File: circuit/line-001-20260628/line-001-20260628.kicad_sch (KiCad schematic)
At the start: 200 parts, among them J1 Conn_01x02_Pin, J2 Conn_01x02_Pin, J3 Conn_02x03_Odd_Even, P1 USB-typeC, SW1 SW_DPDT, SW2 SW_Push, U1 LM339DR, U10 LM339DR, U11 LM339DR, U12 LM339DR, U13 LM339DR, U14 LM339DR, U15 LM339DR, U16 LM339DR, U17 ATmega2560-16A, U18 CH340G, U2 LM339DR, U3 LM339DR, U4 LM339DR, U5 LM339DR, U6 LM339DR, U7 LM339DR, U8 LM339DR, U9 LM339DR, Y1 16MHz, Y2 12MHz

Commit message: Update ラインセンサ基板の回路図のDR完了
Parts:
- removed C12, C8: 0.1u, symbol Device:C
- removed C13: 10u, symbol Device:C
- removed C17, C18: 100n, symbol Device:C
- removed D10, D16, D17, D18, D19, D2, D20, D26, D27, D28, D29, D30, D36, D37, D38, D39, D4, D40, D46, D47, D48, D49, D50, D56, D57, D58, D59, D6, D60, D66, D67, D69, D70, D71, D72, D8: D_Photo, symbol Device:D_Photo
- removed SW1: SW_DPDT, symbol Switch:SW_DPDT_x2
- added C1, C10, C11, C12, C13, C14, C15, C16, C2, C24, C3, C31, C33, C4, C5, C6, C7, C8, C9: 100n, Capacitor_SMD:C_0805_2012Metric, symbol Device:C_Small
- added D37: D40, LED_SMD:LED_0603_1608Metric, symbol Device:LED_Small
- added D38: D41, LED_SMD:LED_0603_1608Metric, symbol Device:LED_Small
- added Q1, Q10, Q11, Q12, Q13, Q14, Q15, Q16, Q17, Q18, Q19, Q2, Q20, Q21, Q22, Q23, Q24, Q25, Q26, Q27, Q28, Q29, Q3, Q30, Q31, Q32, Q33, Q34, Q35, Q36, Q4, Q5, Q6, Q7, Q8, Q9: NJL7502L, @Thrive_footprint_kicker:NJL7502L, symbol Device:Q_Photo_NPN_CE
- added R79, R80: 330, Resistor_SMD:R_0805_2012Metric, symbol Device:R_Small
- C17: renamed from C10; value C -> 22p; footprint (none) -> Capacitor_SMD:C_0805_2012Metric
- C18: renamed from C9; footprint (none) -> Capacitor_SMD:C_0805_2012Metric
- C19: renamed from C11; value C -> 22p; footprint (none) -> Capacitor_SMD:C_0805_2012Metric
- C20: renamed from C14; value 100u -> 470; footprint (none) -> Capacitor_SMD:C_0805_2012Metric
- C21: renamed from C1; value 10u -> 10μ; footprint (none) -> Capacitor_SMD:C_0805_2012Metric
- C22: renamed from C2; value 10u -> 10μ; footprint (none) -> Capacitor_SMD:C_0805_2012Metric
- C23: renamed from C5; value 0.1u -> 100n; footprint (none) -> Capacitor_SMD:C_0805_2012Metric
- C25: renamed from C6; value 0.1u -> 100n; footprint (none) -> Capacitor_SMD:C_0805_2012Metric
- C26: renamed from C7; value 0.1u -> 100n; footprint (none) -> Capacitor_SMD:C_0805_2012Metric
- C27: renamed from C3; value 10u -> 10μ; footprint (none) -> Capacitor_SMD:C_0805_2012Metric
- C28: renamed from C4; value 10u -> 10μ; footprint (none) -> Capacitor_SMD:C_0805_2012Metric
- C29: renamed from C15; footprint (none) -> Capacitor_SMD:C_0805_2012Metric
- C30: renamed from C16; footprint (none) -> Capacitor_SMD:C_0805_2012Metric
- C32: renamed from C19; footprint (none) -> Capacitor_SMD:C_0805_2012Metric
- D1: footprint (none) -> LED_THT:LED_D3.0mm
- D10: renamed from D15; footprint (none) -> LED_THT:LED_D3.0mm
- D11: renamed from D21; footprint (none) -> LED_THT:LED_D3.0mm
- D12: renamed from D22; footprint (none) -> LED_THT:LED_D3.0mm
- D13: renamed from D23; footprint (none) -> LED_THT:LED_D3.0mm
- D14: renamed from D24; footprint (none) -> LED_THT:LED_D3.0mm
- D15: renamed from D25; footprint (none) -> LED_THT:LED_D3.0mm
- D16: renamed from D31; footprint (none) -> LED_THT:LED_D3.0mm
- D17: renamed from D32; footprint (none) -> LED_THT:LED_D3.0mm
- D18: renamed from D33; footprint (none) -> LED_THT:LED_D3.0mm
- D19: renamed from D34; footprint (none) -> LED_THT:LED_D3.0mm
- D2: renamed from D3; footprint (none) -> LED_THT:LED_D3.0mm
- D20: renamed from D35; footprint (none) -> LED_THT:LED_D3.0mm
- D21: renamed from D41; footprint (none) -> LED_THT:LED_D3.0mm
- D22: renamed from D42; footprint (none) -> LED_THT:LED_D3.0mm
- D23: renamed from D43; footprint (none) -> LED_THT:LED_D3.0mm
- D24: renamed from D44; footprint (none) -> LED_THT:LED_D3.0mm
- D25: renamed from D45; footprint (none) -> LED_THT:LED_D3.0mm
- D26: renamed from D51; footprint (none) -> LED_THT:LED_D3.0mm
- D27: renamed from D52; footprint (none) -> LED_THT:LED_D3.0mm
- D28: renamed from D53; footprint (none) -> LED_THT:LED_D3.0mm
- D29: renamed from D54; footprint (none) -> LED_THT:LED_D3.0mm
- D3: renamed from D5; footprint (none) -> LED_THT:LED_D3.0mm
- D30: renamed from D55; footprint (none) -> LED_THT:LED_D3.0mm
- D31: renamed from D61; footprint (none) -> LED_THT:LED_D3.0mm
- D32: renamed from D62; footprint (none) -> LED_THT:LED_D3.0mm
- D33: renamed from D63; footprint (none) -> LED_THT:LED_D3.0mm
- D34: renamed from D64; footprint (none) -> LED_THT:LED_D3.0mm
- D35: renamed from D65; footprint (none) -> LED_THT:LED_D3.0mm
- D36: renamed from D68; footprint (none) -> LED_THT:LED_D3.0mm
- D4: renamed from D7; footprint (none) -> LED_THT:LED_D3.0mm
- D5: renamed from D9; footprint (none) -> LED_THT:LED_D3.0mm
- D6: renamed from D11; footprint (none) -> LED_THT:LED_D3.0mm
- D7: renamed from D12; footprint (none) -> LED_THT:LED_D3.0mm
- D8: renamed from D13; footprint (none) -> LED_THT:LED_D3.0mm
- D9: renamed from D14; footprint (none) -> LED_THT:LED_D3.0mm
- J1: value Conn_01x02_Pin -> Relay_{Power}
- J2: value Conn_01x02_Pin -> Relay_{Signal}
- J3: value Conn_02x03_Odd_Even -> ICSP_{Arduino}; footprint (none) -> Connector_PinHeader_2.54mm:PinHeader_2x03_P2.54mm_Vertical
- R1: renamed from R2; footprint (none) -> Resistor_SMD:R_0805_2012Metric
- R10, R11, R12, R13, R14, R15, R16, R17, R18, R19, R20, R21, R22, R23, R24, R25, R26, R27, R28, R29, R30, R31, R32, R33, R34, R35, R36, R37, R38, R39, R40, R41, R42, R43, R44, R45, R46, R47, R48, R49, R50, R51, R52, R53, R54, R55, R56, R57, R58, R59, R60, R61, R62, R68, R69, R70, R71, R72: footprint (none) -> Resistor_SMD:R_0805_2012Metric
- R2: renamed from R3; footprint (none) -> Resistor_SMD:R_0805_2012Metric
- R3: renamed from R5; footprint (none) -> Resistor_SMD:R_0805_2012Metric
- R4: renamed from R7; footprint (none) -> Resistor_SMD:R_0805_2012Metric
- R5: renamed from R9; footprint (none) -> Resistor_SMD:R_0805_2012Metric
- R6: renamed from R1; footprint (none) -> Resistor_SMD:R_0805_2012Metric
- R63: renamed from R66; footprint (none) -> Resistor_SMD:R_0805_2012Metric
- R64: renamed from R67; footprint (none) -> Resistor_SMD:R_0805_2012Metric
- R65: renamed from R63; footprint (none) -> Resistor_SMD:R_0805_2012Metric
- R66: renamed from R64; footprint (none) -> Resistor_SMD:R_0805_2012Metric
- R67: renamed from R65; footprint (none) -> Resistor_SMD:R_0805_2012Metric
- R7: renamed from R4; footprint (none) -> Resistor_SMD:R_0805_2012Metric
- R73: renamed from R77; footprint (none) -> Resistor_SMD:R_0805_2012Metric
- R74: renamed from R78; footprint (none) -> Resistor_SMD:R_0805_2012Metric
- R75: renamed from R73; footprint (none) -> Resistor_SMD:R_0805_2012Metric
- R76: renamed from R74; footprint (none) -> Resistor_SMD:R_0805_2012Metric
- R77: renamed from R75; footprint (none) -> Resistor_SMD:R_0805_2012Metric
- R78: renamed from R76; footprint (none) -> Resistor_SMD:R_0805_2012Metric
- R8: renamed from R6; footprint (none) -> Resistor_SMD:R_0805_2012Metric
- R81: renamed from R79; footprint (none) -> Resistor_SMD:R_0805_2012Metric
- R82: renamed from R80; footprint (none) -> Resistor_SMD:R_0805_2012Metric
- R83: renamed from R81; footprint (none) -> Resistor_SMD:R_0805_2012Metric
- R84: renamed from R83; footprint (none) -> Resistor_SMD:R_0805_2012Metric
- R85: renamed from R82; footprint (none) -> Resistor_SMD:R_0805_2012Metric
- R9: renamed from R8; footprint (none) -> Resistor_SMD:R_0805_2012Metric
- SW1: renamed from SW2; value SW_Push -> RESET
- U1, U10, U11, U12, U13, U14, U15, U16, U2, U3, U4, U5, U6, U7, U8, U9: footprint (none) -> Package_SO:SOIC-14_3.9x8.7mm_P1.27mm
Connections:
- net +5V_{Arduino} is gone; now on net +5V_{Line}: C23.1, C25.1, C26.1, U17.10 (VCC), U17.100 (AVCC), U17.31 (VCC), U17.61 (VCC), U17.80 (VCC)
- net +5V_{Line}: now also C1.2, C10.2, C11.2, C12.2, C13.2, C14.2, C15.2, C16.2, C2.2, C3.2, C4.2, C5.2, C6.2, C7.2, C8.2, C9.2, Q1.1 (C), Q10.1 (C), Q11.1 (C), Q12.1 (C), Q13.1 (C), Q14.1 (C), Q15.1 (C), Q16.1 (C), Q17.1 (C), Q18.1 (C), Q19.1 (C), Q2.1 (C), Q20.1 (C), Q21.1 (C), Q22.1 (C), Q23.1 (C), Q24.1 (C), Q25.1 (C), Q26.1 (C), Q27.1 (C), Q28.1 (C), Q29.1 (C), Q3.1 (C), Q30.1 (C), Q31.1 (C), Q32.1 (C), Q33.1 (C), Q34.1 (C), Q35.1 (C), Q36.1 (C), Q4.1 (C), Q5.1 (C), Q6.1 (C), Q7.1 (C), Q8.1 (C), Q9.1 (C)
- net GND: now also C1.1, C10.1, C11.1, C12.1, C13.1, C14.1, C15.1, C16.1, C2.1, C24.2, C3.1, C33.1, C4.1, C5.1, C6.1, C7.1, C8.1, C9.1, D37.1 (K), D38.1 (K)
- net LED1: now also R79.1
- net LED2: now also R80.1
- net RST: now also C31.1
- net linesig10_{raw}: now also Q10.2 (E)
- net linesig11_{raw}: now also Q11.2 (E)
- net linesig12_{raw}: now also Q12.2 (E)
- net linesig13_{raw}: now also Q13.2 (E)
- net linesig14_{raw}: now also Q14.2 (E)
- net linesig15_{raw}: now also Q15.2 (E)
- net linesig16_{raw}: now also Q16.2 (E)
- net linesig17_{raw}: now also Q17.2 (E)
- net linesig18_{raw}: now also Q18.2 (E)
- net linesig19_{raw}: now also Q19.2 (E)
- net linesig1_{raw}: now also Q1.2 (E)
- net linesig20_{raw}: now also Q20.2 (E)
- net linesig21_{raw}: now also Q21.2 (E)
- net linesig22_{raw}: now also Q22.2 (E)
- net linesig23_{raw}: now also Q23.2 (E)
- net linesig24_{raw}: now also Q24.2 (E)
- net linesig25_{raw}: now also Q25.2 (E)
- net linesig26_{raw}: now also Q26.2 (E)
- net linesig27_{raw}: now also Q27.2 (E)
- net linesig28_{raw}: now also Q28.2 (E)
- net linesig29_{raw}: now also Q29.2 (E)
- net linesig2_{raw}: now also Q2.2 (E)
- net linesig30_{raw}: now also Q30.2 (E)
- net linesig31_{raw}: now also Q31.2 (E)
- net linesig32_{raw}: now also Q32.2 (E)
- net linesig33_{analog}: now also Q33.2 (E)
- net linesig34_{analog}: now also Q34.2 (E)
- net linesig35_{analog}: now also Q35.2 (E)
- net linesig36_{analog}: now also Q36.2 (E)
- net linesig3_{raw}: now also Q3.2 (E)
- net linesig4_{raw}: now also Q4.2 (E)
- net linesig5_{raw}: now also Q5.2 (E)
- net linesig6_{raw}: now also Q6.2 (E)
- net linesig7_{raw}: now also Q7.2 (E)
- net linesig8_{raw}: now also Q8.2 (E)
- net linesig9_{raw}: now also Q9.2 (E)
- net at R85.1, U18.13 (~{DTR}): now also C31.2
- net at U18.4 (V3): now also C33.2
- net at U17.98 (AREF): now also C24.1
- new net: D38.2 (A), R80.2
- new net: D37.2 (A), R79.2
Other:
- moved on the sheet: C17, C18, C19, C20, C21, C22, C23, C25, C26, C27, C28, C29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

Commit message: Update 470Fを470μFにした
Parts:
- C20: value 470 -> 470μ
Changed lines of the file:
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@@
 			)
 		)
-		(property "Value" "470"
+		(property "Value" "470μ"
 			(at 331.47 228.6 0)
 			(show_name no)

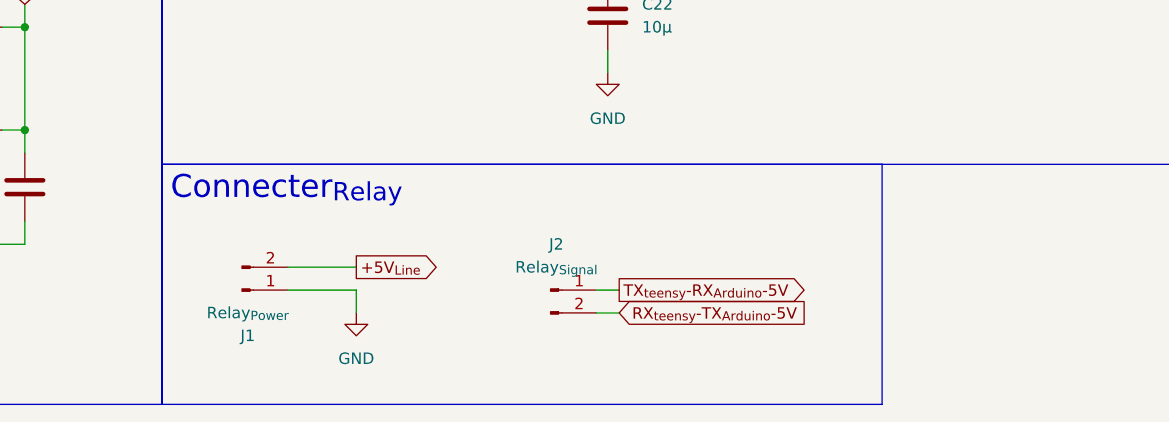
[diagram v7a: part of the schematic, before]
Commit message: Update ラインセンサ基板の回路図のシンボル-フットプリントの紐づけを完了させた
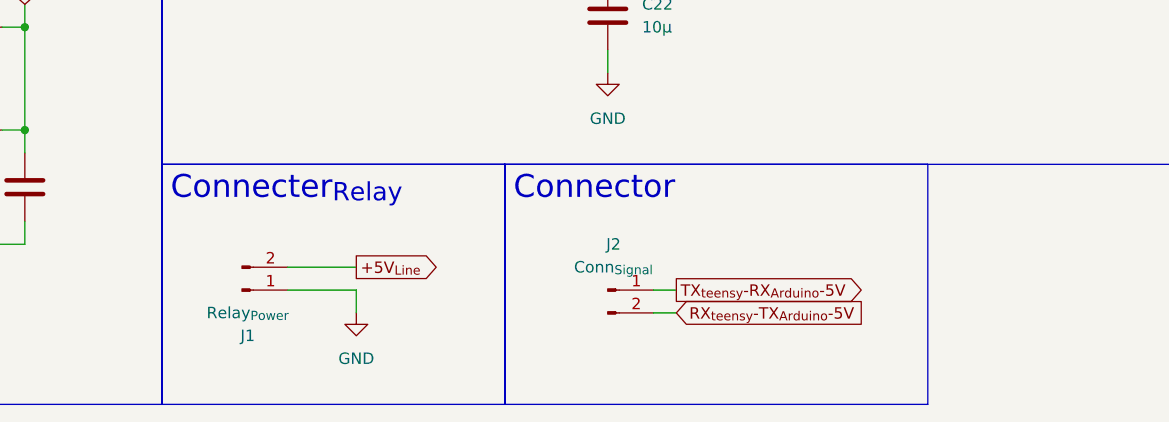
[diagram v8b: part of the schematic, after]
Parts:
- J1: footprint (none) -> Connector_AMASS:AMASS_XT30U-M_1x02_P5.0mm_Vertical
- J2: value Relay_{Signal} -> Conn_{Signal}; footprint (none) -> @Thrive_footprint_line:Conn_01x02_Wire_Only
- SW1: footprint (none) -> @Thrive_footprint_line:TVBP06-B043C
- Y1, Y2: footprint (none) -> Crystal:Crystal_HC49-4H_Vertical
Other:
- moved on the sheet: J2
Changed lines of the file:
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@@
 		(exclude_from_sim no)
 		(at 304.8 304.8 0)
-		(size 80.01 26.67)
+		(size 38.1 26.67)
 		(margins 0.9525 0.9525 0.9525 0.9525)
 		(stroke
@@
 		)
 	)
+	(text_box "Connector"
+		(exclude_from_sim no)
+		(at 342.9 304.8 0)
+		(size 46.99 26.67)
+		(margins 0.9525 0.9525 0.9525 0.9525)
+		(stroke
+			(width 0)
+			(type solid)
+		)
+		(fill
+			(type none)
+		)
+		(effects
+			(font
+				(size 2.54 2.54)
+			)
+			(justify left top)
+		)
+	)
 	(text_box "USB"
 		(exclude_from_sim no)
@@
 	(wire
 		(pts
-			(xy 353.06 321.31) (xy 355.6 321.31)
+			(xy 359.41 321.31) (xy 361.95 321.31)
 		)
 		(stroke
@@
 	(wire
 		(pts
-			(xy 353.06 318.77) (xy 355.6 318.77)
+			(xy 359.41 318.77) (xy 361.95 318.77)
 		)
 		(stroke
@@
 	(global_label "RX_{teensy}-TX_{Arduino}-5V"
 		(shape input)
-		(at 355.6 321.31 0)
+		(at 361.95 321.31 0)
 		(fields_autoplaced yes)
 		(effects
@@
 		)
 		(property "Intersheetrefs" "${INTERSHEET_REFS}"
-			(at 373.7268 321.31 0)
+			(at 380.0768 321.31 0)
 			(hide yes)
 			(show_name no)
@@
 	(global_label "TX_{teensy}-RX_{Arduino}-5V"
 		(shape output)
-		(at 355.6 318.77 0)
+		(at 361.95 318.77 0)
 		(fields_autoplaced yes)
 		(effects
@@
 		)
 		(property "Intersheetrefs" "${INTERSHEET_REFS}"
-			(at 373.7267 318.77 0)
+			(at 380.0767 318.77 0)
 			(hide yes)
 			(show_name no)
@@
 			)
 		)
-		(property "Footprint" ""
+		(property "Footprint" "@Thrive_footprint_line:TVBP06-B043C"
 			(at 271.78 238.76 0)
 			(hide yes)
@@
 	(symbol
 		(lib_id "Connector:Conn_01x02_Pin")
-		(at 347.98 318.77 0)
+		(at 354.33 318.77 0)
 		(unit 1)
 		(body_style 1)
@@
 		(fields_autoplaced yes)
 		(property "Reference" "J2"
-			(at 348.615 313.69 0)
+			(at 354.965 313.69 0)
 			(show_name no)
 			(do_not_autoplace no)
@@
 			)
 		)
-		(property "Value" "Relay_{Signal}"
-			(at 348.615 316.23 0)
+		(property "Value" "Conn_{Signal}"
+			(at 354.965 316.23 0)
 			(show_name no)
 			(do_not_autoplace no)
@@
 			)
 		)
-		(property "Footprint" ""
-			(at 347.98 318.77 0)
+		(property "Footprint" "@Thrive_footprint_line:Conn_01x02_Wire_Only"
+			(at 354.33 318.77 0)
 			(hide yes)
 			(show_name no)
@@
 		)
 		(property "Datasheet" ""
-			(at 347.98 318.77 0)
+			(at 354.33 318.77 0)
 			(hide yes)
 			(show_name no)
@@
 		)
 		(property "Description" "Generic connector, single row, 01x02, script generated"
-			(at 347.98 318.77 0)
+			(at 354.33 318.77 0)
 			(hide yes)
 			(show_name no)
@@
 			)
 		)
-		(property "Footprint" ""
+		(property "Footprint" "Connector_AMASS:AMASS_XT30U-M_1x02_P5.0mm_Vertical"
 			(at 313.69 318.77 0)
 			(hide yes)
@@
 			)
 		)
-		(property "Footprint" ""
+		(property "Footprint" "Crystal:Crystal_HC49-4H_Vertical"
 			(at 283.21 300.99 0)
 			(hide yes)
@@
 			)
 		)
-		(property "Footprint" ""
+		(property "Footprint" "Crystal:Crystal_HC49-4H_Vertical"
 			(at 488.95 128.27 0)
 			(hide yes)
